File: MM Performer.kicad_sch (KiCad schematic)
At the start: 41 parts, among them IC1 68000D, J1 VCC, J2 GND, U1 MC68030RC, U2 MC68881FN-SOC, U3 ATF16V8BJ, U4 ATF16V8BJ, U5 ATF16V8BJ, U6 ATF16V8BJ, U7 ATF16V8BJ

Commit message: Begin cleanup of the traces for the new revision
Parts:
- SJ1: footprint Jumper:SolderJumper-2_P1.3mm_Open_TrianglePad1.0x1.5mm -> Connector_PinHeader_2.54mm:PinHeader_1x02_P2.54mm_Vertical
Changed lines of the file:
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@@
 			)
 		)
-		(property "Footprint" "Jumper:SolderJumper-2_P1.3mm_Open_TrianglePad1.0x1.5mm"
+		(property "Footprint" "Connector_PinHeader_2.54mm:PinHeader_1x02_P2.54mm_Vertical"
 			(at 142.24 121.92 0)
 			(effects

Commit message: Reorganize placement on the PCB
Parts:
- added C12, C13, C14: 100nF, Capacitor_SMD:C_1206_3216Metric_Pad1.33x1.80mm_HandSolder, symbol MM Performer-eagle-import:C-EUC1206
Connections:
- net GND: now also C12.2, C13.2, C14.2
- net VCC: now also C12.1, C13.1, C14.1

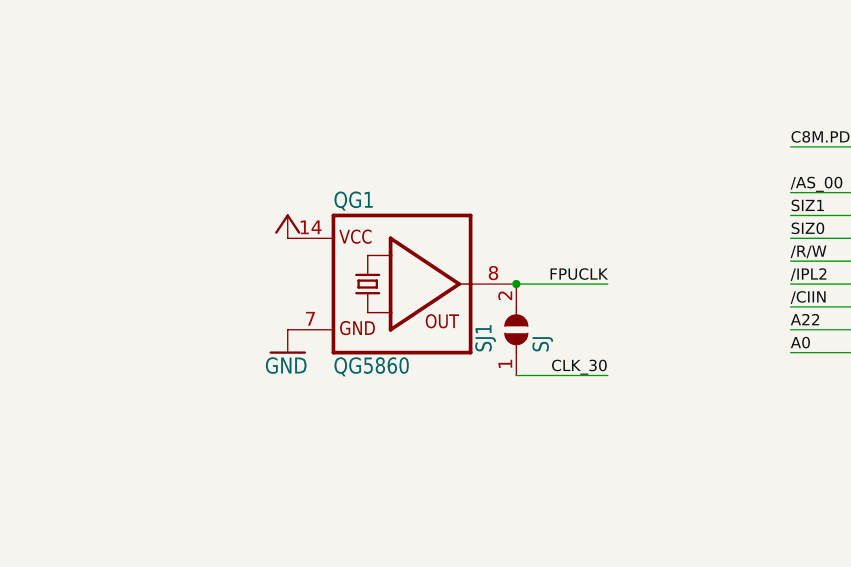
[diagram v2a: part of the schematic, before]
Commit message: Some rerouting of traces
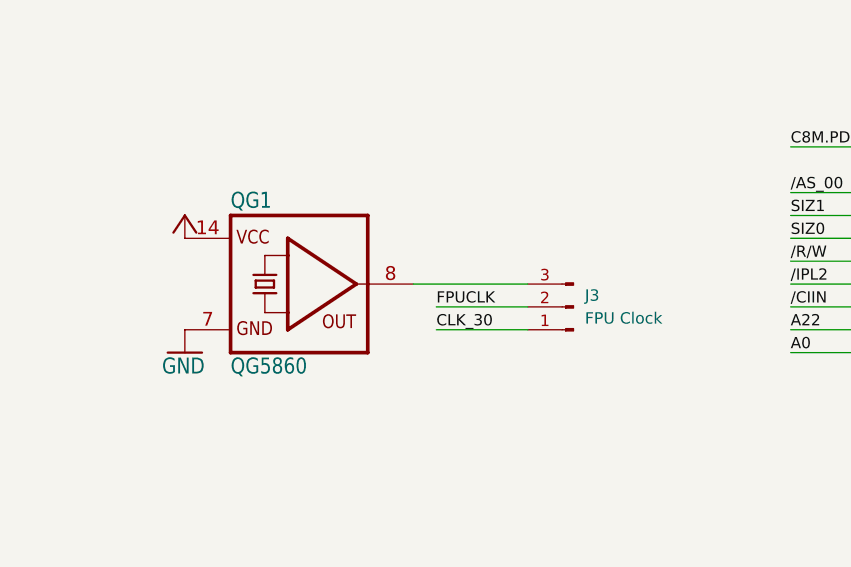
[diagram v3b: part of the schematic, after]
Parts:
- removed SJ1: SJ, Connector_PinHeader_2.54mm:PinHeader_1x02_P2.54mm_Vertical, symbol MM Performer-eagle-import:SJ
- added J3: FPU Clock, Connector_PinHeader_2.54mm:PinHeader_1x03_P2.54mm_Vertical, symbol Connector:Conn_01x03_Pin
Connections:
- net CLK_30: now also J3.1 (Pin_1)
- net FPUCLK: now also J3.2 (Pin_2); no longer QG1.8 (OUT)
- new net: J3.3 (Pin_3), QG1.8 (OUT)
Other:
- moved on the sheet: QG1

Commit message: Import revision 2 board
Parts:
- removed J1: VCC, TestPoint:TestPoint_THTPad_4.0x4.0mm_Drill2.0mm, symbol Connector_Generic:Conn_01x01
- removed J2: GND, TestPoint:TestPoint_THTPad_4.0x4.0mm_Drill2.0mm, symbol Connector_Generic:Conn_01x01
- IC1: value 68000D -> 68000
- U1: value MC68030RC -> 68030
- U2: value MC68881FN-SOC -> 68882
- U3, U4, U5, U6, U7: value ATF16V8BJ -> GAL16V8
- renumbered J3 to J1
